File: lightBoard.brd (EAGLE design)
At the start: 68.2 x 36.4 mm, 26 parts, among them U1 LED-TRICOLOR-5050, U10 LED-TRICOLOR-5050, U11 LED-TRICOLOR-5050, U12 LED-TRICOLOR-5050, U2 LED-TRICOLOR-5050, U3 LED-TRICOLOR-5050, U4 LED-TRICOLOR-5050, U5 LED-TRICOLOR-5050, U6 LED-TRICOLOR-5050, U7 LED-TRICOLOR-5050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

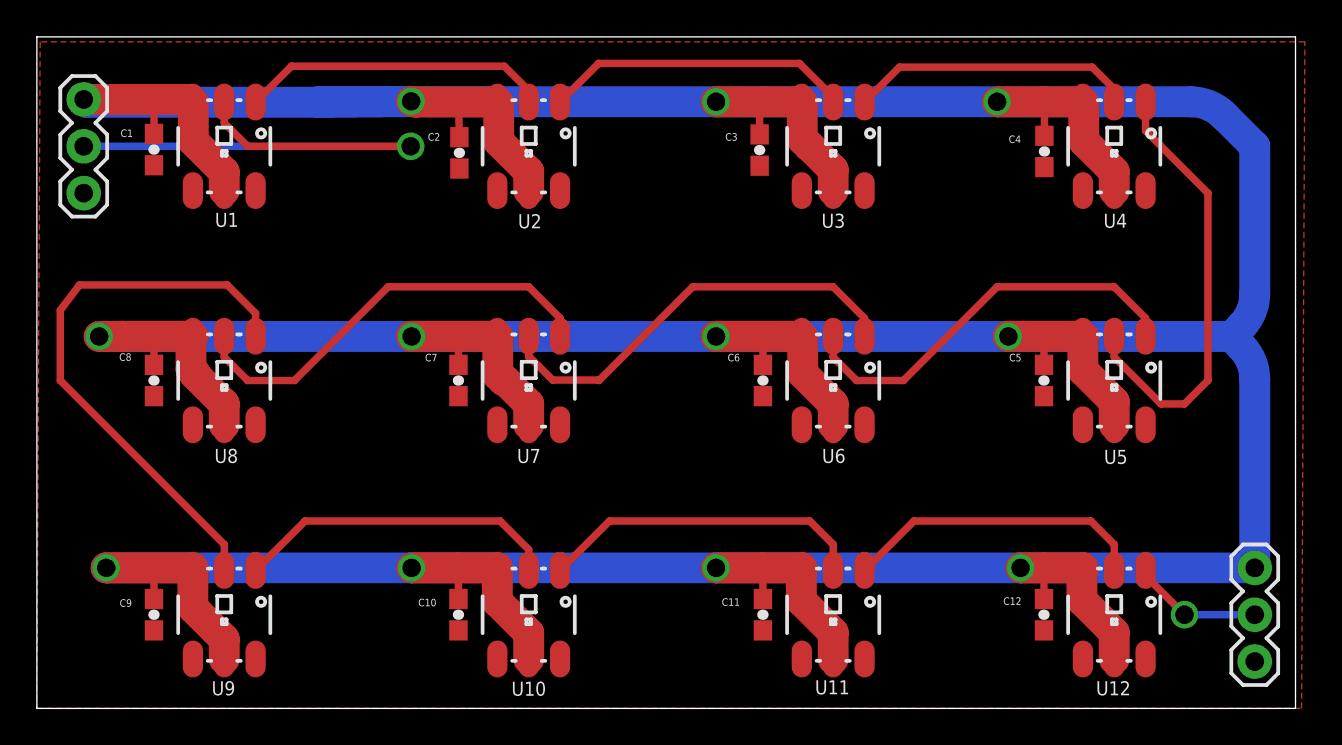
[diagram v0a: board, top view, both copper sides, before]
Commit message: Updated board with no 90 degree angles
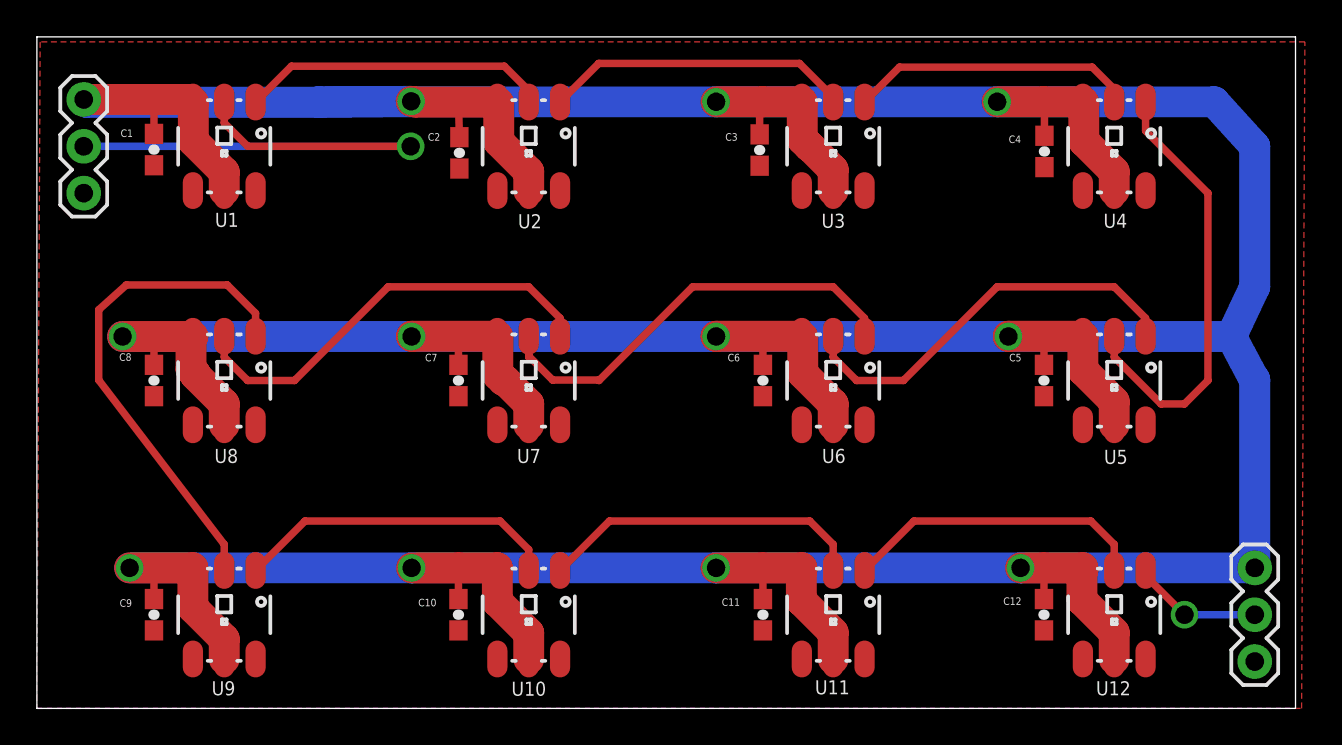
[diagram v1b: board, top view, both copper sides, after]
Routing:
- net VCC: track 374.3 -> 368.8 mm
- net N$10: track 30.9 -> 27.3 mm
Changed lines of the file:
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@@
 <wire x1="59.0296" y1="62.0776" x2="43.18" y2="62.0776" width="1.6764" layer="16"/>
 <wire x1="43.18" y1="62.0776" x2="26.67" y2="62.0776" width="1.6764" layer="16"/>
-<wire x1="26.67" y1="62.0776" x2="9.7282" y2="62.0776" width="1.6764" layer="16"/>
+<wire x1="26.67" y1="62.0776" x2="10.9982" y2="62.0776" width="1.6764" layer="16"/>
 <wire x1="59.0296" y1="62.0776" x2="71.12" y2="62.0776" width="1.6764" layer="16"/>
-<wire x1="14.81" y1="62.09" x2="10.9982" y2="62.09" width="1.6764" layer="1"/>
-<wire x1="10.9982" y1="62.09" x2="9.7282" y2="62.0776" width="1.6764" layer="1"/>
-<via x="9.7282" y="62.0776" extent="1-16" drill="1"/>
+<via x="10.9982" y="62.0776" extent="1-16" drill="1"/>
 <wire x1="31.32" y1="62.09" x2="26.67" y2="62.09" width="1.6764" layer="1"/>
 <wire x1="26.67" y1="62.09" x2="26.67" y2="62.0776" width="1.6764" layer="1"/>
@@
 <wire x1="14.9352" y1="60.071" x2="14.7066" y2="60.2996" width="1.6764" layer="1"/>
 <wire x1="14.7066" y1="60.2996" x2="14.7066" y2="61.9866" width="1.6764" layer="1"/>
-<wire x1="14.7066" y1="61.9866" x2="14.81" y2="62.09" width="1.6764" layer="1"/>
+<wire x1="14.7066" y1="61.9866" x2="14.7976" y2="62.0776" width="1.6764" layer="1"/>
+<wire x1="14.7976" y1="62.0776" x2="14.81" y2="62.09" width="1.6764" layer="1"/>
 <wire x1="33.02" y1="57.29" x2="33.02" y2="58.42" width="1.6764" layer="1"/>
 <wire x1="33.02" y1="58.42" x2="31.75" y2="59.69" width="1.6764" layer="1"/>
@@
 <wire x1="59.69" y1="49.53" x2="43.18" y2="49.53" width="1.6764" layer="16"/>
 <wire x1="43.18" y1="49.53" x2="26.67" y2="49.53" width="1.6764" layer="16"/>
-<wire x1="26.67" y1="49.53" x2="10.1092" y2="49.53" width="1.6764" layer="16"/>
+<wire x1="26.67" y1="49.53" x2="11.3792" y2="49.53" width="1.6764" layer="16"/>
 <wire x1="14.81" y1="49.4284" x2="14.81" y2="49.53" width="1.6764" layer="1"/>
-<wire x1="14.81" y1="49.53" x2="10.1092" y2="49.53" width="1.6764" layer="1"/>
-<via x="10.1092" y="49.53" extent="1-16" drill="1"/>
-<wire x1="10.1092" y1="49.53" x2="10.16" y2="49.53" width="1.6764" layer="16"/>
+<wire x1="14.81" y1="49.53" x2="11.3792" y2="49.53" width="1.6764" layer="1"/>
+<via x="11.3792" y="49.53" extent="1-16" drill="1"/>
 <wire x1="31.32" y1="49.39" x2="31.32" y2="49.53" width="1.6764" layer="1"/>
 <wire x1="31.32" y1="49.53" x2="29.21" y2="49.53" width="1.6764" layer="1"/>
@@
 <wire x1="63.0682" y1="60.2488" x2="63.0682" y2="62.0882" width="1.6764" layer="1"/>
 <wire x1="63.0682" y1="62.0882" x2="63.07" y2="62.09" width="1.6764" layer="1"/>
-<wire x1="10.9982" y1="62.09" x2="10.9982" y2="62.23" width="0.4064" layer="1"/>
-<wire x1="10.9982" y1="62.23" x2="11.43" y2="62.23" width="0.4064" layer="1"/>
 <wire x1="12.7" y1="62.09" x2="14.81" y2="62.09" width="0.4064" layer="1"/>
 <wire x1="31.32" y1="62.09" x2="31.32" y2="62.0776" width="0.4064" layer="1"/>
@@
 <wire x1="14.8336" y1="72.6694" x2="14.8336" y2="74.7664" width="1.6764" layer="1"/>
 <wire x1="14.8336" y1="74.7664" x2="14.81" y2="74.79" width="1.6764" layer="1"/>
-<wire x1="58.42" y1="74.803" x2="68.924896875" y2="74.803" width="1.6764" layer="16"/>
-<wire x1="68.924896875" y1="74.803" x2="70.72095" y2="74.05905" width="1.6764" layer="16" curve="-45.00005"/>
-<wire x1="70.72095" y1="74.05905" x2="72.39" y2="72.39" width="1.6764" layer="16"/>
-<wire x1="72.39" y1="72.39" x2="72.39" y2="64.399703125" width="1.6764" layer="16"/>
-<wire x1="72.39" y1="64.399703125" x2="71.64605" y2="62.60365" width="1.6764" layer="16" curve="-45.00005"/>
-<wire x1="71.64605" y1="62.60365" x2="71.12" y2="62.0776" width="1.6764" layer="16"/>
-<wire x1="71.12" y1="62.0776" x2="71.64605" y2="61.55155" width="1.6764" layer="16"/>
-<wire x1="71.64605" y1="61.55155" x2="72.39" y2="59.755496875" width="1.6764" layer="16" curve="-45.00007"/>
-<wire x1="72.39" y1="59.755496875" x2="72.39" y2="49.53" width="1.6764" layer="16"/>
+<wire x1="58.42" y1="74.803" x2="70.194896875" y2="74.803" width="1.6764" layer="16"/>
+<wire x1="72.39" y1="72.39" x2="72.39" y2="64.77" width="1.6764" layer="16"/>
+<wire x1="72.39" y1="59.755496875" x2="72.39" y2="59.69" width="1.6764" layer="16"/>
+<wire x1="72.39" y1="59.69" x2="72.39" y2="49.53" width="1.6764" layer="16"/>
+<wire x1="71.12" y1="62.0776" x2="72.39" y2="64.77" width="1.6764" layer="16"/>
+<wire x1="71.12" y1="62.0776" x2="72.39" y2="59.69" width="1.6764" layer="16"/>
+<wire x1="70.194896875" y1="74.803" x2="72.39" y2="72.39" width="1.6764" layer="16"/>
+<wire x1="14.7976" y1="62.0776" x2="10.9982" y2="62.0776" width="1.6764" layer="1"/>
 </signal>
 <signal name="GND">
@@
 <contactref element="U8" pad="1"/>
 <contactref element="U9" pad="2" route="any" routetag="DI"/>
-<wire x1="7.62" y1="63.5" x2="7.62" y2="59.69" width="0.4064" layer="1"/>
-<wire x1="7.62" y1="59.69" x2="16.51" y2="50.8" width="0.4064" layer="1"/>
+<wire x1="9.7028" y1="63.5254" x2="9.7028" y2="59.7154" width="0.4064" layer="1"/>
+<wire x1="9.7028" y1="59.7154" x2="16.51" y2="50.8" width="0.4064" layer="1"/>
 <wire x1="16.51" y1="50.8" x2="16.51" y2="49.39" width="0.4064" layer="1"/>
-<wire x1="16.673" y1="64.8716" x2="8.6614" y2="64.8716" width="0.4064" layer="1"/>
-<wire x1="8.6614" y1="64.8716" x2="7.62" y2="63.5" width="0.4064" layer="1"/>
+<wire x1="16.673" y1="64.8716" x2="11.2014" y2="64.8716" width="0.4064" layer="1"/>
+<wire x1="11.2014" y1="64.8716" x2="9.7028" y2="63.5254" width="0.4064" layer="1"/>
 <wire x1="16.673" y1="64.8716" x2="18.21" y2="63.3346" width="0.4064" layer="1"/>
 <wire x1="18.21" y1="63.3346" x2="18.21" y2="62.09" width="0.4064" layer="1"/>
